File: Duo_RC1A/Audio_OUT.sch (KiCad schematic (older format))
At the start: 45 parts, among them J3 JACK_P10_TRS_6P, J4 JACK_P10_TRS_6P, J5 JACK_P10_TRS_6P, K1 IMC03TS, K2 IMC03TS, Q1 BS870, Q2 BS870, Q3 BS870

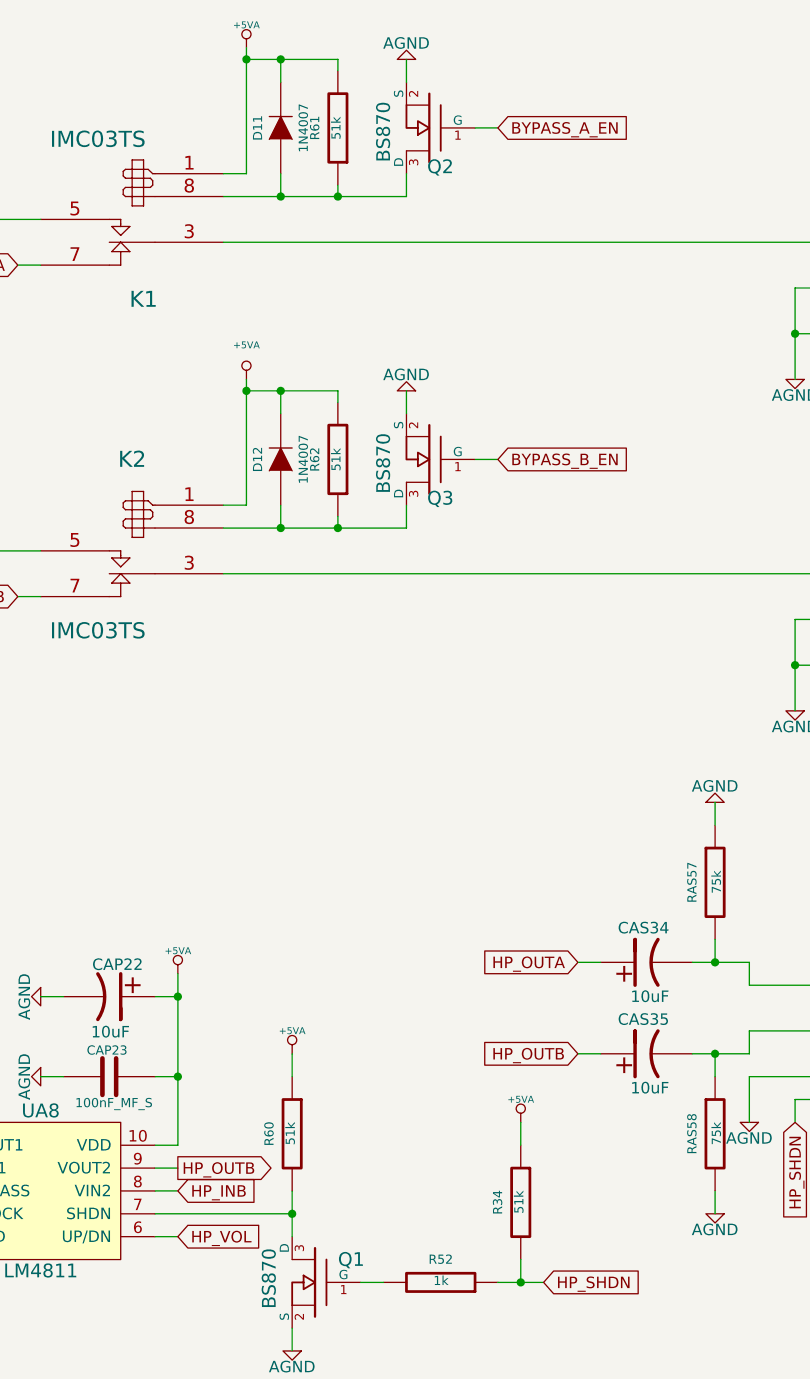
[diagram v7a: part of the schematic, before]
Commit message: Changed the LCD for the 2.8pol. Rotated the bottom board connector. Moved the 3.3V linear regulator from the bottom board to the top board, and changed the power for the top board from 3.3V to 9V.
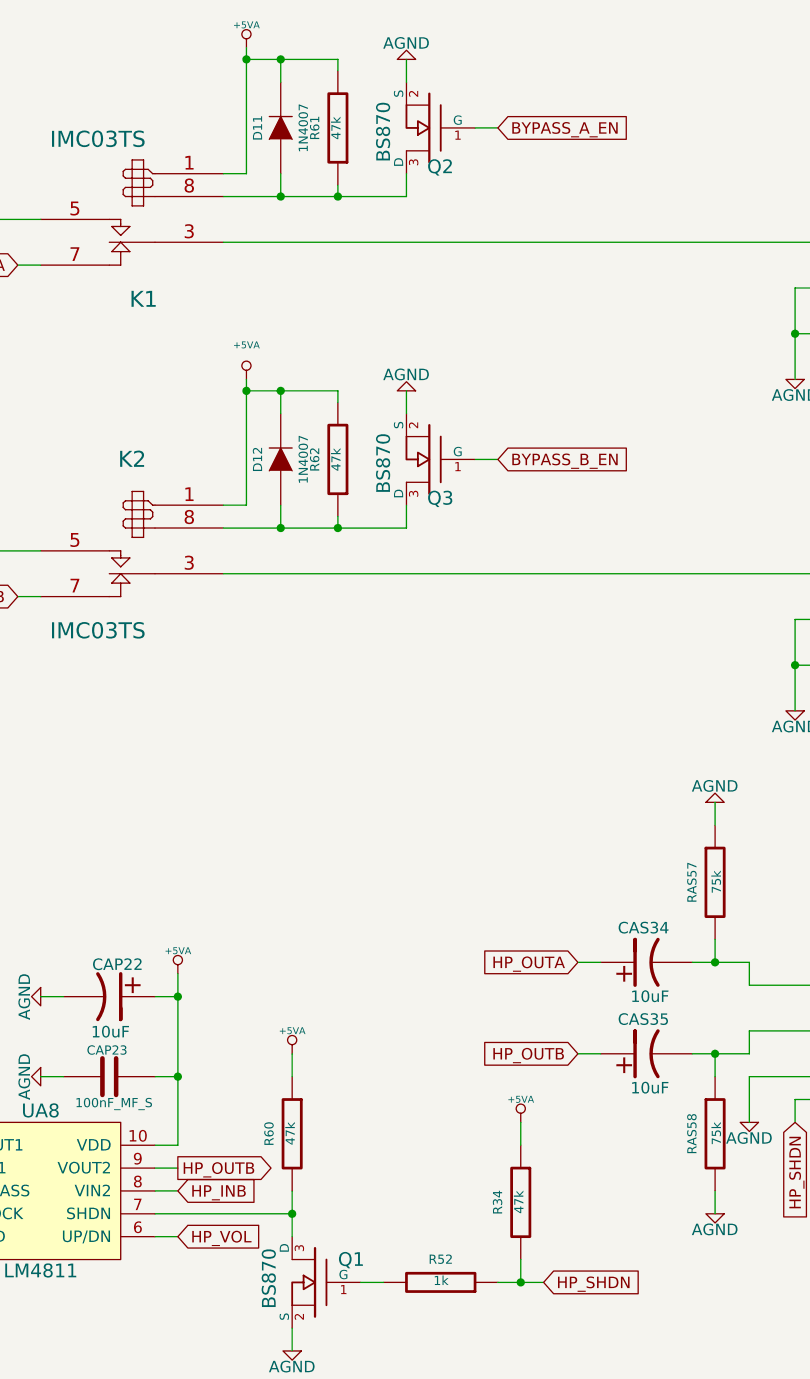
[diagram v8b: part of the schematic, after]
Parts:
- CAS25, CAS26, CAS27, CAS28: footprint Duo_Audio_HMI_RC1A:CapacitorMetalFilm_7.2x2.5MM_P5MM -> Duo_Audio_HMI_RC1A:CapacitorMetalFilm_7.2x4.5MM_P5MM
- R34, R60, R61, R62: value 51k -> 47k
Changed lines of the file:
@@
 $EndDescr
 $Comp
-L AGND #PWR0157
+L AGND #PWR0152
 U 1 1 5324F6FB
 P 9900 2100
-F 0 "#PWR0157" H 9900 2100 40  0001 C CNN
+F 0 "#PWR0152" H 9900 2100 40  0001 C CNN
 F 1 "AGND" H 9900 2030 50  0000 C CNN
 F 2 "~" H 9900 2100 60  0000 C CNN
@@
 $EndComp
 $Comp
-L AGND #PWR0158
+L AGND #PWR0153
 U 1 1 5324F705
 P 9900 3550
-F 0 "#PWR0158" H 9900 3550 40  0001 C CNN
+F 0 "#PWR0153" H 9900 3550 40  0001 C CNN
 F 1 "AGND" H 9900 3480 50  0000 C CNN
 F 2 "~" H 9900 3550 60  0000 C CNN
@@
 P 7900 1000
 F 0 "R61" V 8000 1000 40  0000 C CNN
-F 1 "51k" V 7907 1001 40  0000 C CNN
+F 1 "47k" V 7907 1001 40  0000 C CNN
 F 2 "Duo_Audio_HMI_RC1A:SM0603" V 7830 1000 30  0001 C CNN
 F 3 "~" H 7900 1000 30  0000 C CNN
@@
 P 7900 2450
 F 0 "R62" V 8000 2450 40  0000 C CNN
-F 1 "51k" V 7907 2451 40  0000 C CNN
+F 1 "47k" V 7907 2451 40  0000 C CNN
 F 2 "Duo_Audio_HMI_RC1A:SM0603" V 7830 2450 30  0001 C CNN
 F 3 "~" H 7900 2450 30  0000 C CNN
@@
 BYPASS_A_EN
 $Comp
-L AGND #PWR0159
+L AGND #PWR0154
 U 1 1 534031A9
 P 8200 700
-F 0 "#PWR0159" H 8200 700 40  0001 C CNN
+F 0 "#PWR0154" H 8200 700 40  0001 C CNN
 F 1 "AGND" H 8200 630 50  0000 C CNN
 F 2 "~" H 8200 700 60  0000 C CNN
@@
 BYPASS_B_EN
 $Comp
-L AGND #PWR0160
+L AGND #PWR0155
 U 1 1 53403913
 P 8200 2150
-F 0 "#PWR0160" H 8200 2150 40  0001 C CNN
+F 0 "#PWR0155" H 8200 2150 40  0001 C CNN
 F 1 "AGND" H 8200 2080 50  0000 C CNN
 F 2 "~" H 8200 2150 60  0000 C CNN
@@
 $EndComp
 $Comp
-L +5VA #PWR0161
+L +5VA #PWR0156
 U 1 1 5342DE35
 P 7500 650
-F 0 "#PWR0161" H 7500 780 20  0001 C CNN
+F 0 "#PWR0156" H 7500 780 20  0001 C CNN
 F 1 "+5VA" H 7500 750 30  0000 C CNN
 F 2 "" H 7500 650 60  0000 C CNN
@@
 $EndComp
 $Comp
-L +5VA #PWR0162
+L +5VA #PWR0157
 U 1 1 5342DE42
 P 7500 2100
-F 0 "#PWR0162" H 7500 2230 20  0001 C CNN
+F 0 "#PWR0157" H 7500 2230 20  0001 C CNN
 F 1 "+5VA" H 7500 2250 30  0000 C CNN
 F 2 "" H 7500 2100 60  0000 C CNN
@@
 $EndComp
 $Comp
-L AGND #PWR0163
+L AGND #PWR0158
 U 1 1 5345439A
 P 2650 1800
-F 0 "#PWR0163" H 2650 1800 40  0001 C CNN
+F 0 "#PWR0158" H 2650 1800 40  0001 C CNN
 F 1 "AGND" H 2650 1730 50  0000 C CNN
 F 2 "~" H 2650 1800 60  0000 C CNN
@@
 $EndComp
 $Comp
-L VCC_AMP_AUDIO #PWR0164
+L VCC_AMP_AUDIO #PWR0159
 U 1 1 5345491A
 P 2650 900
-F 0 "#PWR0164" H 2650 1000 30  0001 C CNN
+F 0 "#PWR0159" H 2650 1000 30  0001 C CNN
 F 1 "VCC_AMP_AUDIO" H 2650 1000 30  0000 C CNN
 F 2 "~" H 2650 900 60  0000 C CNN
@@
 $EndComp
 $Comp
-L AGND #PWR0165
+L AGND #PWR0160
 U 1 1 5345497D
 P 2050 1000
-F 0 "#PWR0165" H 2050 1000 40  0001 C CNN
+F 0 "#PWR0160" H 2050 1000 40  0001 C CNN
 F 1 "AGND" H 2050 930 50  0000 C CNN
 F 2 "~" H 2050 1000 60  0000 C CNN
@@
 $EndComp
 $Comp
-L AGND #PWR0166
+L AGND #PWR0161
 U 1 1 53454F2A
 P 4500 2100
-F 0 "#PWR0166" H 4500 2100 40  0001 C CNN
+F 0 "#PWR0161" H 4500 2100 40  0001 C CNN
 F 1 "AGND" H 4500 2030 50  0000 C CNN
 F 2 "~" H 4500 2100 60  0000 C CNN
@@
 $EndComp
 $Comp
-L AGND #PWR0167
+L AGND #PWR0162
 U 1 1 53457462
 P 4500 3550
-F 0 "#PWR0167" H 4500 3550 40  0001 C CNN
+F 0 "#PWR0162" H 4500 3550 40  0001 C CNN
 F 1 "AGND" H 4500 3480 50  0000 C CNN
 F 2 "~" H 4500 3550 60  0000 C CNN
@@
 $EndComp
 $Comp
-L AGND #PWR0168
+L AGND #PWR0163
 U 1 1 536BB908
 P 9700 5350
-F 0 "#PWR0168" H 9700 5350 40  0001 C CNN
+F 0 "#PWR0163" H 9700 5350 40  0001 C CNN
 F 1 "AGND" H 9700 5280 50  0000 C CNN
 F 2 "~" H 9700 5350 60  0000 C CNN
@@
 F 0 "CAS25" V 3050 2000 40  0000 L CNN
 F 1 "470pF_MF" V 2750 1950 40  0000 L CNN
-F 2 "Duo_Audio_HMI_RC1A:CapacitorMetalFilm_7.2x2.5MM_P5MM" H 2938 1950 30  0001 C CNN
+F 2 "Duo_Audio_HMI_RC1A:CapacitorMetalFilm_7.2x4.5MM_P5MM" H 2938 1950 30  0001 C CNN
 F 3 "~" H 2900 2100 60  0000 C CNN
 	1    2900 2100
@@
 F 0 "CAS26" V 3050 3450 40  0000 L CNN
 F 1 "470pF_MF" V 2750 3400 40  0000 L CNN
-F 2 "Duo_Audio_HMI_RC1A:CapacitorMetalFilm_7.2x2.5MM_P5MM" H 2938 3400 30  0001 C CNN
+F 2 "Duo_Audio_HMI_RC1A:CapacitorMetalFilm_7.2x4.5MM_P5MM" H 2938 3400 30  0001 C CNN
 F 3 "~" H 2900 3550 60  0000 C CNN
 	1    2900 3550
@@
 $EndComp
 $Comp
-L AGND #PWR0169
+L AGND #PWR0164
 U 1 1 536D7789
 P 2650 5100
-F 0 "#PWR0169" H 2650 5100 40  0001 C CNN
+F 0 "#PWR0164" H 2650 5100 40  0001 C CNN
 F 1 "AGND" H 2650 5030 50  0000 C CNN
 F 2 "~" H 2650 5100 60  0000 C CNN
@@
 $EndComp
 $Comp
-L VCC_AMP_AUDIO #PWR0170
+L VCC_AMP_AUDIO #PWR0165
 U 1 1 536D778F
 P 2650 4200
-F 0 "#PWR0170" H 2650 4300 30  0001 C CNN
+F 0 "#PWR0165" H 2650 4300 30  0001 C CNN
 F 1 "VCC_AMP_AUDIO" H 2650 4300 30  0000 C CNN
 F 2 "~" H 2650 4200 60  0000 C CNN
@@
 $EndComp
 $Comp
-L AGND #PWR0171
+L AGND #PWR0166
 U 1 1 536D779B
 P 2050 4300
-F 0 "#PWR0171" H 2050 4300 40  0001 C CNN
+F 0 "#PWR0166" H 2050 4300 40  0001 C CNN
 F 1 "AGND" H 2050 4230 50  0000 C CNN
 F 2 "~" H 2050 4300 60  0000 C CNN
@@
 F 0 "CAS27" V 3050 5300 40  0000 L CNN
 F 1 "470pF_MF" V 2750 5250 40  0000 L CNN
-F 2 "Duo_Audio_HMI_RC1A:CapacitorMetalFilm_7.2x2.5MM_P5MM" H 2938 5250 30  0001 C CNN
+F 2 "Duo_Audio_HMI_RC1A:CapacitorMetalFilm_7.2x4.5MM_P5MM" H 2938 5250 30  0001 C CNN
 F 3 "~" H 2900 5400 60  0000 C CNN
 	1    2900 5400
@@
 F 0 "CAS28" V 3050 6750 40  0000 L CNN
 F 1 "470pF_MF" V 2750 6700 40  0000 L CNN
-F 2 "Duo_Audio_HMI_RC1A:CapacitorMetalFilm_7.2x2.5MM_P5MM" H 2938 6700 30  0001 C CNN
+F 2 "Duo_Audio_HMI_RC1A:CapacitorMetalFilm_7.2x4.5MM_P5MM" H 2938 6700 30  0001 C CNN
 F 3 "~" H 2900 6850 60  0000 C CNN
 	1    2900 6850
@@
 HP_INB
 $Comp
-L +5VA #PWR0172
+L +5VA #PWR0167
 U 1 1 536D1E09
 P 7200 4700
-F 0 "#PWR0172" H 7200 4830 20  0001 C CNN
+F 0 "#PWR0167" H 7200 4830 20  0001 C CNN
 F 1 "+5VA" H 7200 4800 30  0000 C CNN
 F 2 "" H 7200 4700 60  0000 C CNN
@@
 $EndComp
 $Comp
-L AGND #PWR0173
+L AGND #PWR0168
 U 1 1 536D2358
 P 6600 5150
-F 0 "#PWR0173" H 6600 5150 40  0001 C CNN
+F 0 "#PWR0168" H 6600 5150 40  0001 C CNN
 F 1 "AGND" H 6600 5080 50  0000 C CNN
 F 2 "~" H 6600 5150 60  0000 C CNN
@@
 HP_OUTB
 $Comp
-L AGND #PWR0174
+L AGND #PWR0169
 U 1 1 536D33CF
 P 5000 5650
-F 0 "#PWR0174" H 5000 5650 40  0001 C CNN
+F 0 "#PWR0169" H 5000 5650 40  0001 C CNN
 F 1 "AGND" H 5000 5580 50  0000 C CNN
 F 2 "~" H 5000 5650 60  0000 C CNN
@@
 $EndComp
 $Comp
-L AGND #PWR0175
+L AGND #PWR0170
 U 1 1 536D345C
 P 6000 5950
-F 0 "#PWR0175" H 6000 5950 40  0001 C CNN
+F 0 "#PWR0170" H 6000 5950 40  0001 C CNN
 F 1 "AGND" H 6000 5880 50  0000 C CNN
 F 2 "~" H 6000 5950 60  0000 C CNN
@@
 P 7700 5400
 F 0 "R60" V 7800 5400 40  0000 C CNN
-F 1 "51k" V 7707 5401 40  0000 C CNN
+F 1 "47k" V 7707 5401 40  0000 C CNN
 F 2 "Duo_Audio_HMI_RC1A:SM0603" V 7630 5400 30  0001 C CNN
 F 3 "~" H 7700 5400 30  0000 C CNN
@@
 $EndComp
 $Comp
-L +5VA #PWR0176
+L +5VA #PWR0171
 U 1 1 536DFBA9
 P 7700 5050
-F 0 "#PWR0176" H 7700 5180 20  0001 C CNN
+F 0 "#PWR0171" H 7700 5180 20  0001 C CNN
 F 1 "+5VA" H 7700 5150 30  0000 C CNN
 F 2 "" H 7700 5050 60  0000 C CNN
@@
 $EndComp
 $Comp
-L AGND #PWR0177
+L AGND #PWR0172
 U 1 1 5373D101
 P 6600 4800
-F 0 "#PWR0177" H 6600 4800 40  0001 C CNN
+F 0 "#PWR0172" H 6600 4800 40  0001 C CNN
 F 1 "AGND" H 6600 4730 50  0000 C CNN
 F 2 "~" H 6600 4800 60  0000 C CNN
@@
 $EndComp
 $Comp
-L AGND #PWR0178
+L AGND #PWR0173
 U 1 1 5384BAEF
 P 9550 5750
-F 0 "#PWR0178" H 9550 5750 40  0001 C CNN
+F 0 "#PWR0173" H 9550 5750 40  0001 C CNN
 F 1 "AGND" H 9550 5680 50  0000 C CNN
 F 2 "~" H 9550 5750 60  0000 C CNN
@@
 $EndComp
 $Comp
-L AGND #PWR0179
+L AGND #PWR0174
 U 1 1 5384BBB9
 P 9550 3950
-F 0 "#PWR0179" H 9550 3950 40  0001 C CNN
+F 0 "#PWR0174" H 9550 3950 40  0001 C CNN
 F 1 "AGND" H 9550 3880 50  0000 C CNN
 F 2 "~" H 9550 3950 60  0000 C CNN
@@
 $EndComp
 $Comp
-L AGND #PWR0180
+L AGND #PWR0175
 U 1 1 53864F9B
 P 7700 6350
-F 0 "#PWR0180" H 7700 6350 40  0001 C CNN
+F 0 "#PWR0175" H 7700 6350 40  0001 C CNN
 F 1 "AGND" H 7700 6280 50  0000 C CNN
 F 2 "~" H 7700 6350 60  0000 C CNN
@@
 P 8700 5700
 F 0 "R34" V 8800 5700 40  0000 C CNN
-F 1 "51k" V 8707 5701 40  0000 C CNN
+F 1 "47k" V 8707 5701 40  0000 C CNN
 F 2 "Duo_Audio_HMI_RC1A:SM0603" V 8630 5700 30  0001 C CNN
 F 3 "~" H 8700 5700 30  0000 C CNN
@@
 	8700 6050 8700 5950
 $Comp
-L +5VA #PWR0181
+L +5VA #PWR0176
 U 1 1 53865E7E
 P 8700 5350
-F 0 "#PWR0181" H 8700 5480 20  0001 C CNN
+F 0 "#PWR0176" H 8700 5480 20  0001 C CNN
 F 1 "+5VA" H 8700 5450 30  0000 C CNN
 F 2 "" H 8700 5350 60  0000 C CNN
